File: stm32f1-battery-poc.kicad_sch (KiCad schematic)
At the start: 19 parts, among them J1 Conn_02x07_Odd_Even, SW1 SW_Push, SW2 SW_Push, U1 STM32F103C8Tx, Y1 8M

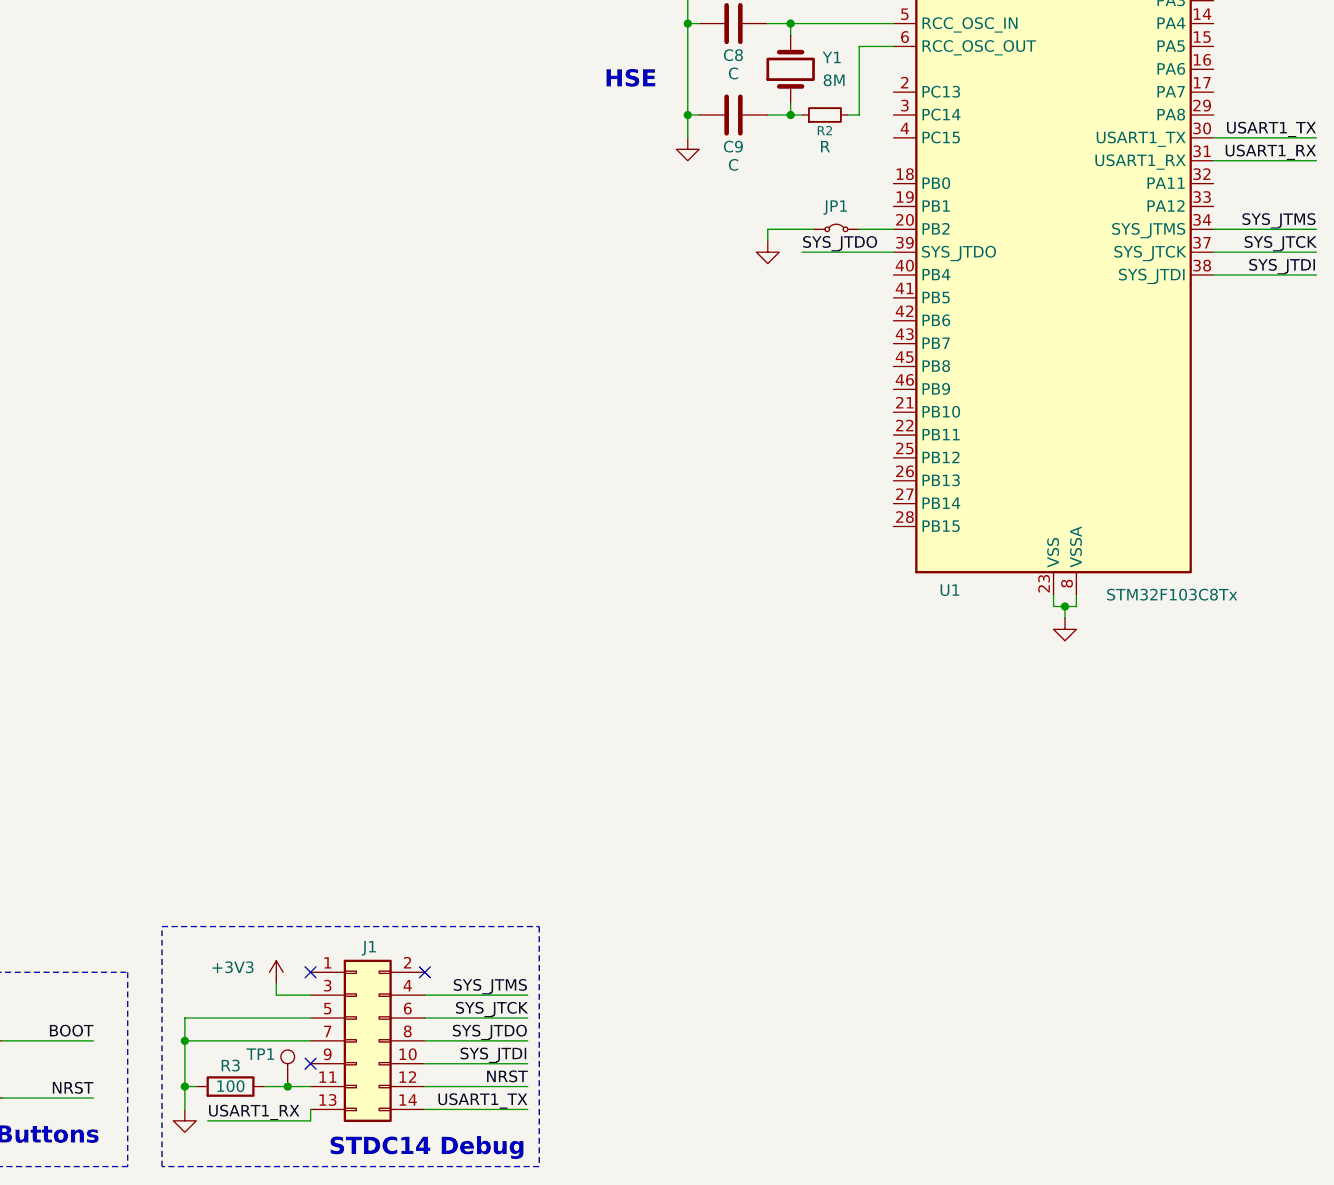
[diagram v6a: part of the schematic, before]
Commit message: schem: add SN65HVD230 CAN transceiver
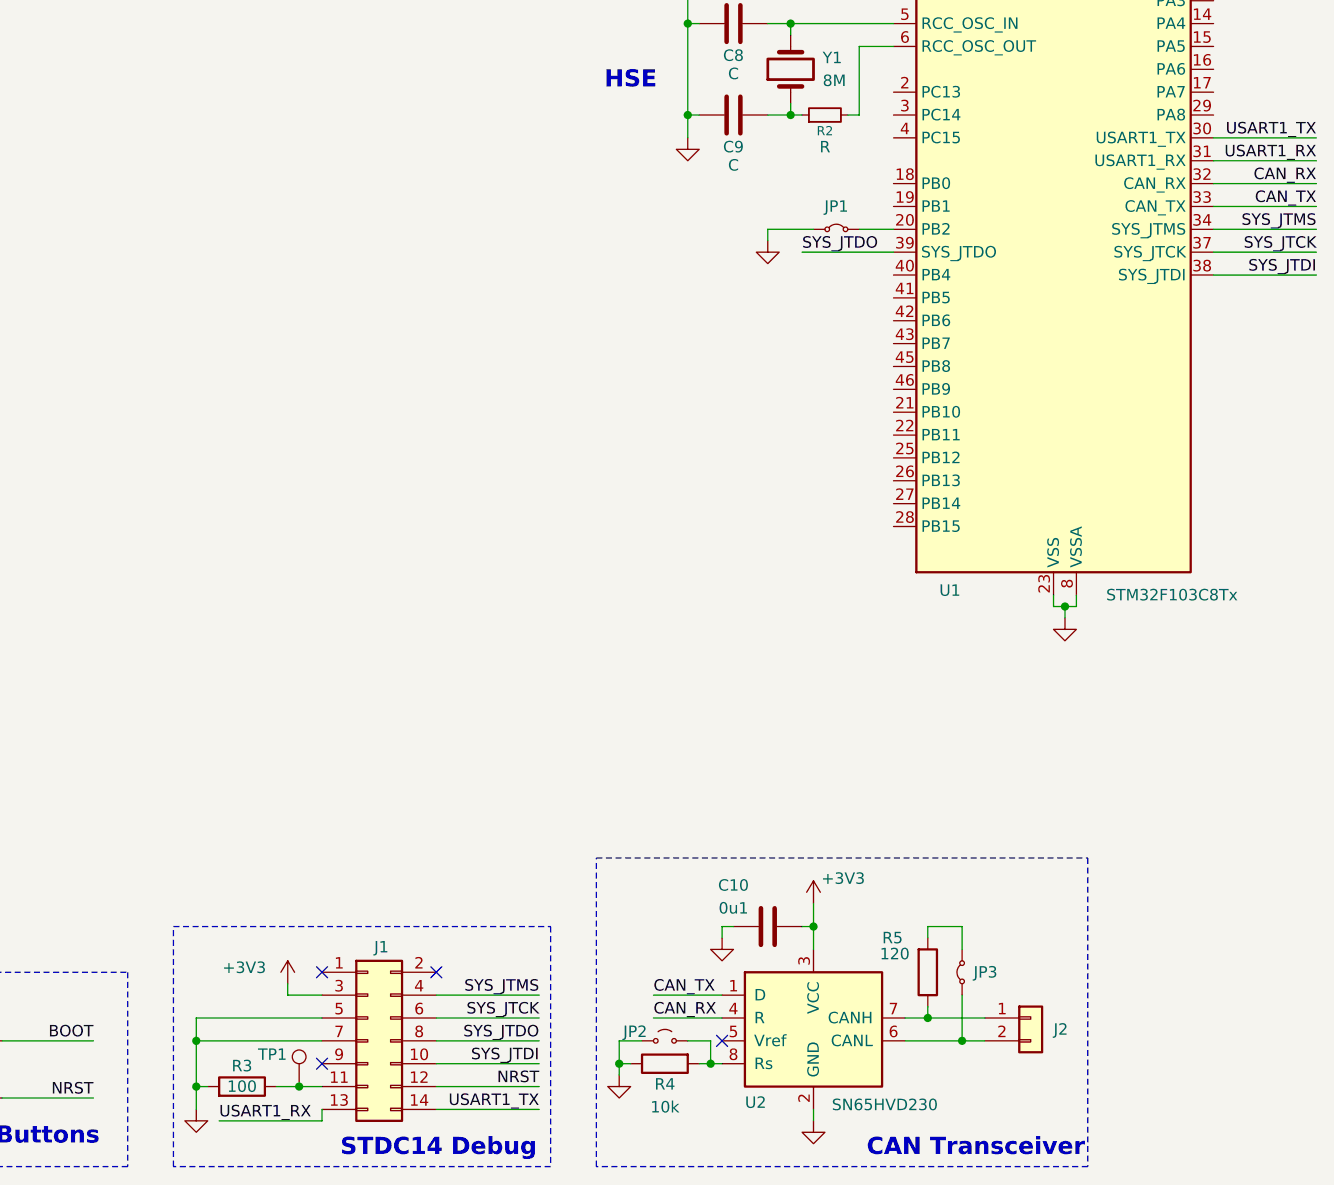
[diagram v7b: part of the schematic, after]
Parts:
- added C10: 0u1, symbol Device:C
- added J2: Conn_01x02, symbol Connector_Generic:Conn_01x02
- added JP2: Jumper_2_Small_Open, symbol Jumper:Jumper_2_Small_Open
- added JP3: Jumper_2_Small_Bridged, symbol Jumper:Jumper_2_Small_Bridged
- added R4: 10k, symbol Device:R
- added R5: 120, symbol Device:R
- added U2: SN65HVD230, Package_SO:SOIC-8_3.9x4.9mm_P1.27mm, symbol Interface_CAN_LIN:SN65HVD230
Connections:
- net +3V3: now also C10.1, U2.3 (VCC)
- net GND: now also C10.2, JP2.1 (A), R4.1, U2.2 (GND)
- net CAN_RX: now reaches U1.32 (PA11)
- net CAN_RX: now also U2.4 (R)
- net CAN_TX: now reaches U1.33 (PA12)
- net CAN_TX: now also U2.1 (D)
- new net: J2.1 (Pin_1), R5.1, U2.7 (CANH)
- new net: JP3.2 (B), R5.2
- new net: J2.2 (Pin_2), JP3.1 (A), U2.6 (CANL)
- new net: JP2.2 (B), R4.2, U2.8 (Rs)
- no-connect marks 3 -> 4
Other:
- note added: "CAN Transceiver"
- moved on the sheet: J1, R3, TP1

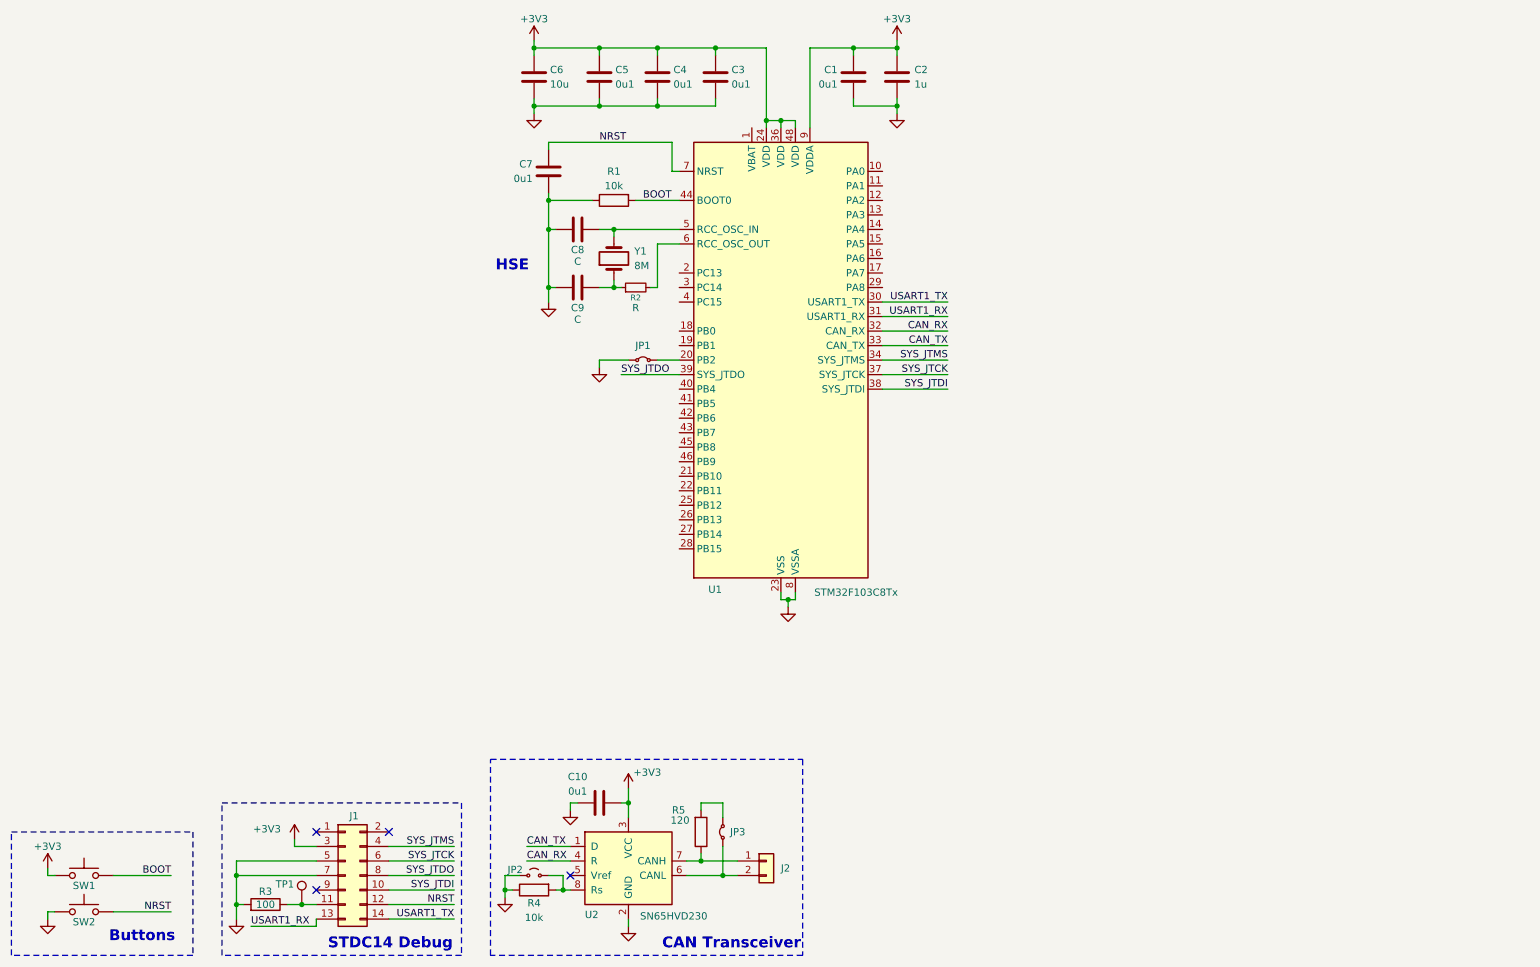
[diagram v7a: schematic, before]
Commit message: schem: add BQ77905 Battery protection
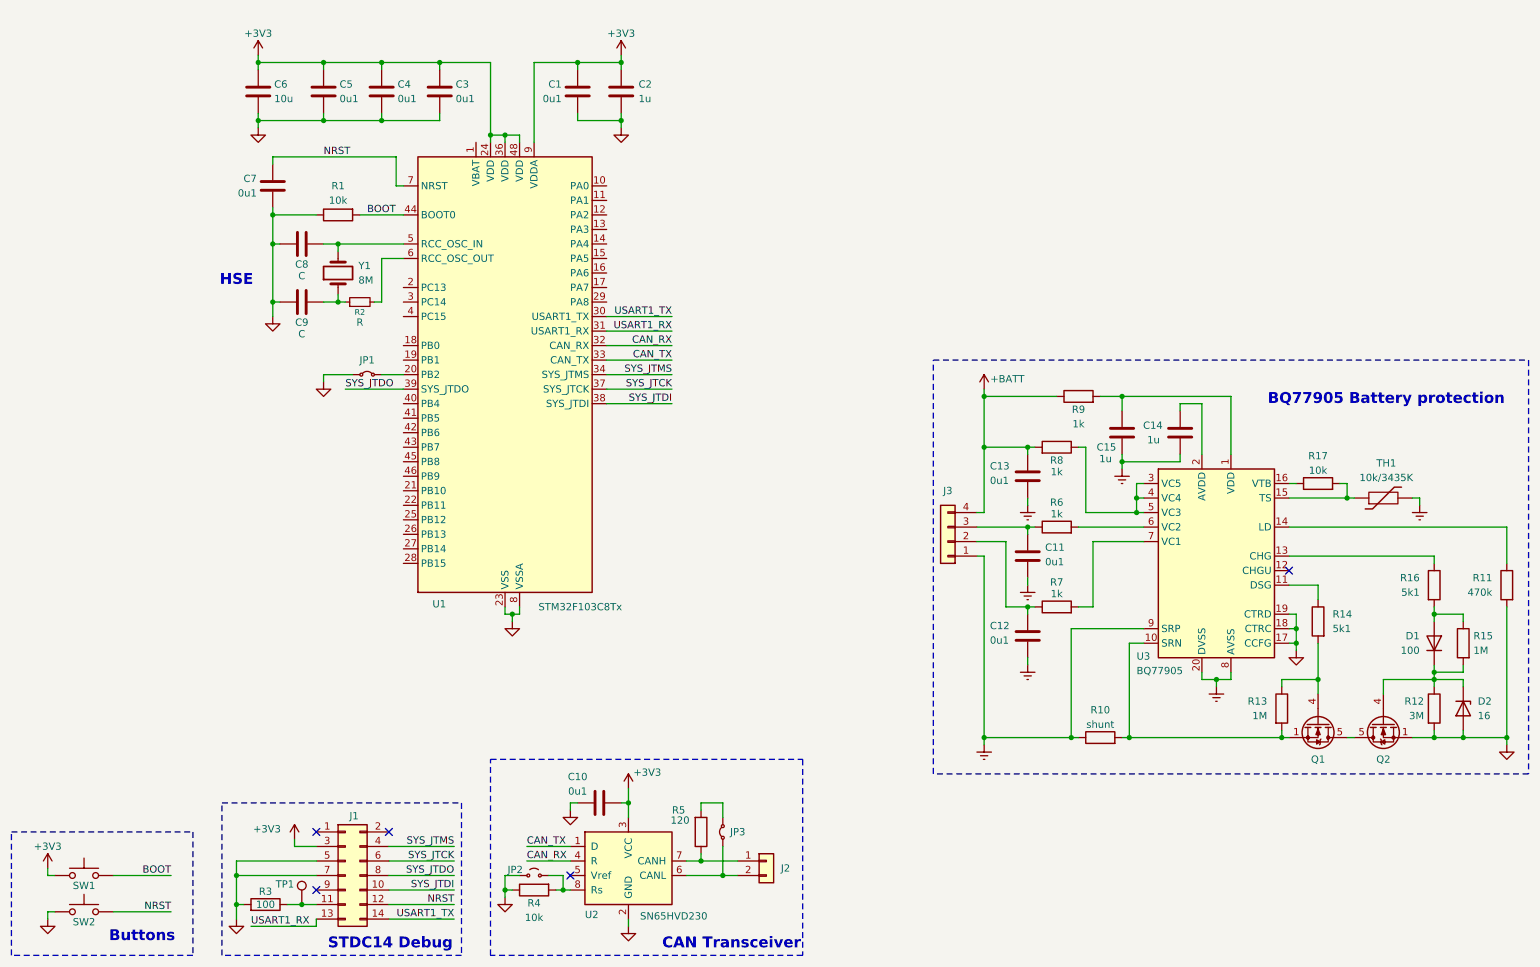
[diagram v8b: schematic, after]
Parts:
- added C11, C12, C13: 0u1, symbol Device:C
- added C14, C15: 1u, symbol Device:C
- added D1: 100, Diode_SMD:D_SOD-323, symbol Device:D
- added D2: 16, Diode_SMD:D_SOD-123, symbol Device:D_Zener
- added J3: Conn_01x04, symbol Connector_Generic:Conn_01x04
- added Q1, Q2: Q_NMOS, Package_SO:Vishay_PowerPAK_1212-8_Single, symbol Transistor_FET:SiS454DN
- added R10: shunt, symbol Device:R
- added R11: 470k, symbol Device:R
- added R12: 3M, symbol Device:R
- added R13, R15: 1M, symbol Device:R
- added R14, R16: 5k1, Resistor_SMD:R_0402_1005Metric, symbol Device:R
- added R17: 10k, symbol Device:R
- added R6, R7, R8, R9: 1k, symbol Device:R
- added TH1: 10k/3435K, symbol Device:Thermistor
- added U3: BQ77905, Package_SO:TSSOP-20_4.4x6.5mm_P0.65mm, symbol GLCS:BQ77905
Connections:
- net GND: now also D2.2 (A), Q2.1 (S), Q2.2 (S), Q2.3 (S), R11.2, R12.2, U3.17 (CCFG), U3.18 (CTRC), U3.19 (CTRD)
- new net: D1.2 (A), R15.1, R16.2
- new net: D1.1 (K), D2.1 (K), Q2.4 (G), R12.1, R15.2
- new net: R14.1, U3.11 (DSG)
- new net: Q1.4 (G), R13.1, R14.2
- new net: C11.1, J3.3 (Pin_3), R6.1
- new net: R6.2, U3.6 (VC2)
- new net: C14.2, U3.2 (AVDD)
- new net: C15.2, R9.2, U3.1 (VDD)
- new net: Q1.1 (S), Q1.2 (S), Q1.3 (S), R10.2, R13.2, U3.10 (SRN)
- new net: R16.1, U3.13 (CHG)
- new net: R11.1, U3.14 (LD)
- new net: R17.2, TH1.1, U3.15 (TS)
- new net: R17.1, U3.16 (VTB)
- new net: R8.1, U3.3 (VC5), U3.4 (VC4), U3.5 (VC3)
- new net: R7.2, U3.7 (VC1)
- new net: C12.1, J3.2 (Pin_2), R7.1
- new net: Q1.5 (D), Q2.5 (D)
- new net +BATT: C13.1, J3.4 (Pin_4), R8.2, R9.1
- new net BGND: C11.2, C12.2, C13.2, C14.1, C15.1, J3.1 (Pin_1), R10.1, TH1.2, U3.20 (DVSS), U3.8 (AVSS), U3.9 (SRP)
- no-connect marks 4 -> 5
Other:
- note added: "BQ77905 Battery protection"
- moved on the sheet: C1, C2, C3, C4, C5, C6, C7, C8, C9, JP1, R1, R2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
